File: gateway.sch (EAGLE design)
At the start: 25 parts, among them J1 RASPBERRYPI-40-PIN-GPIO_PTH_N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, Q1 BSS123

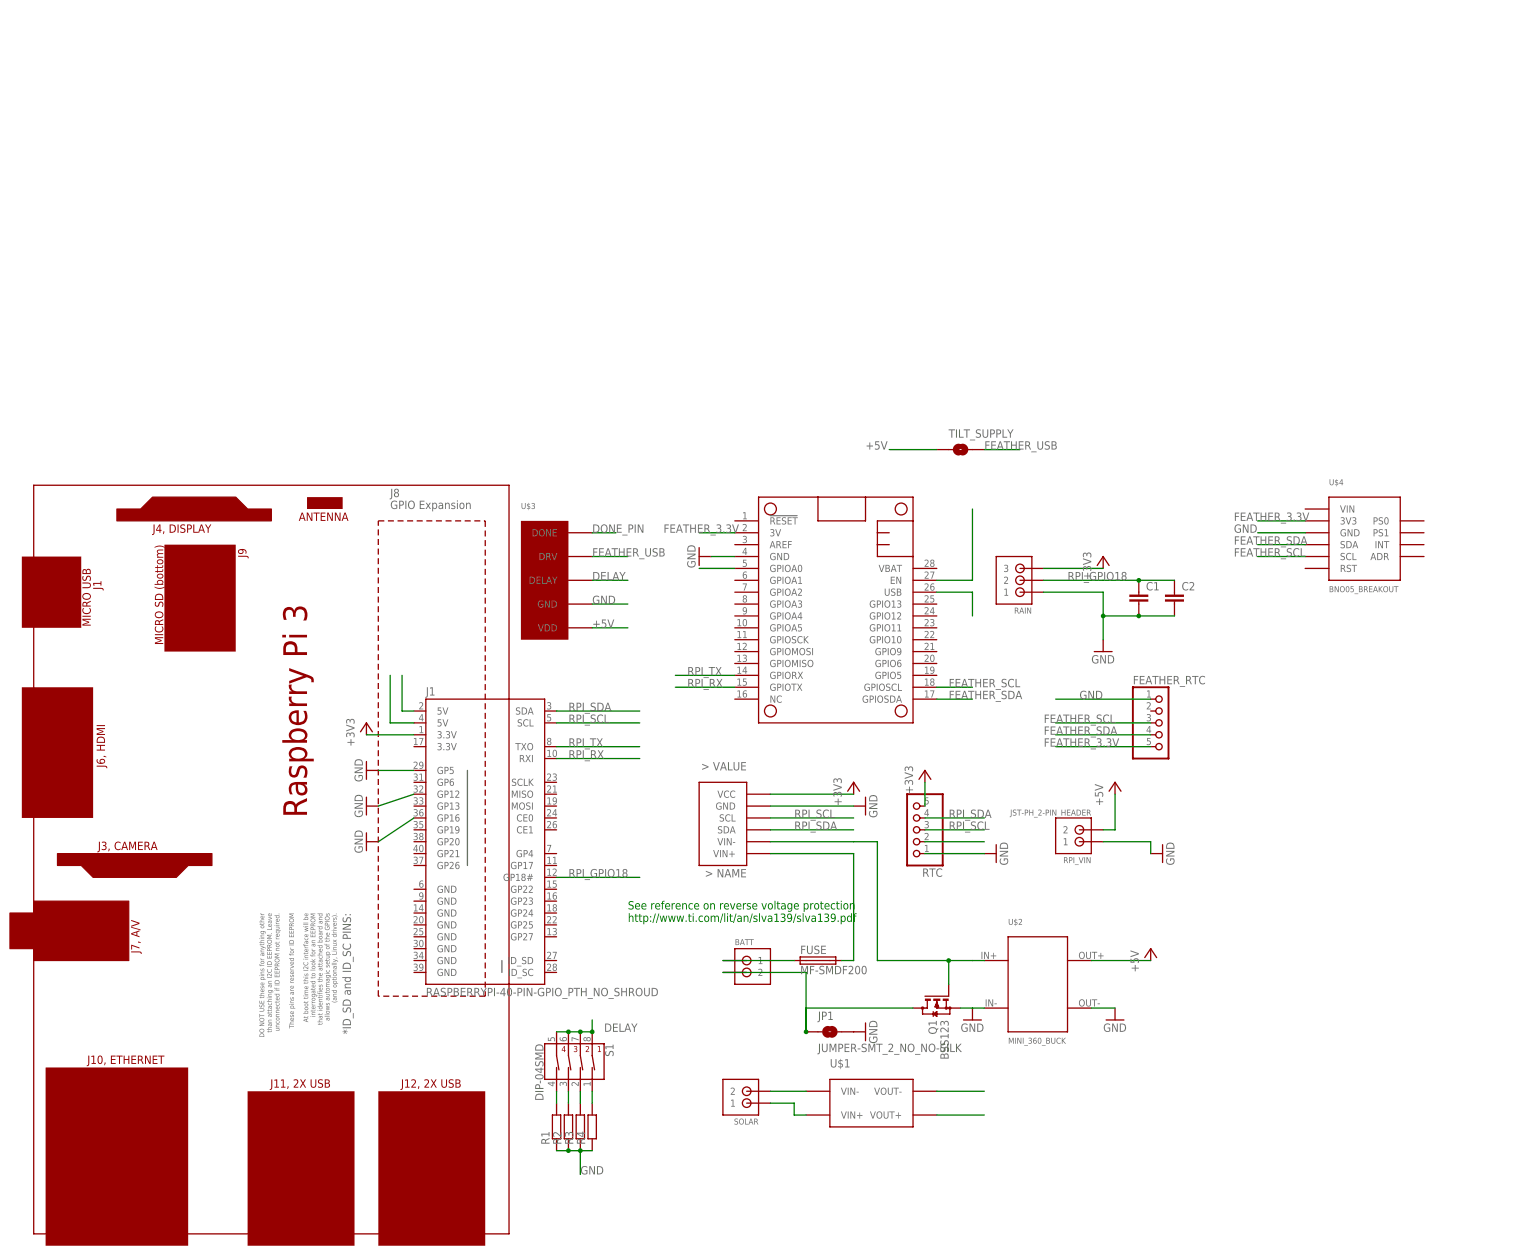
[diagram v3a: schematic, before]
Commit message: added pads to the microcontrollers ( feather and pi )
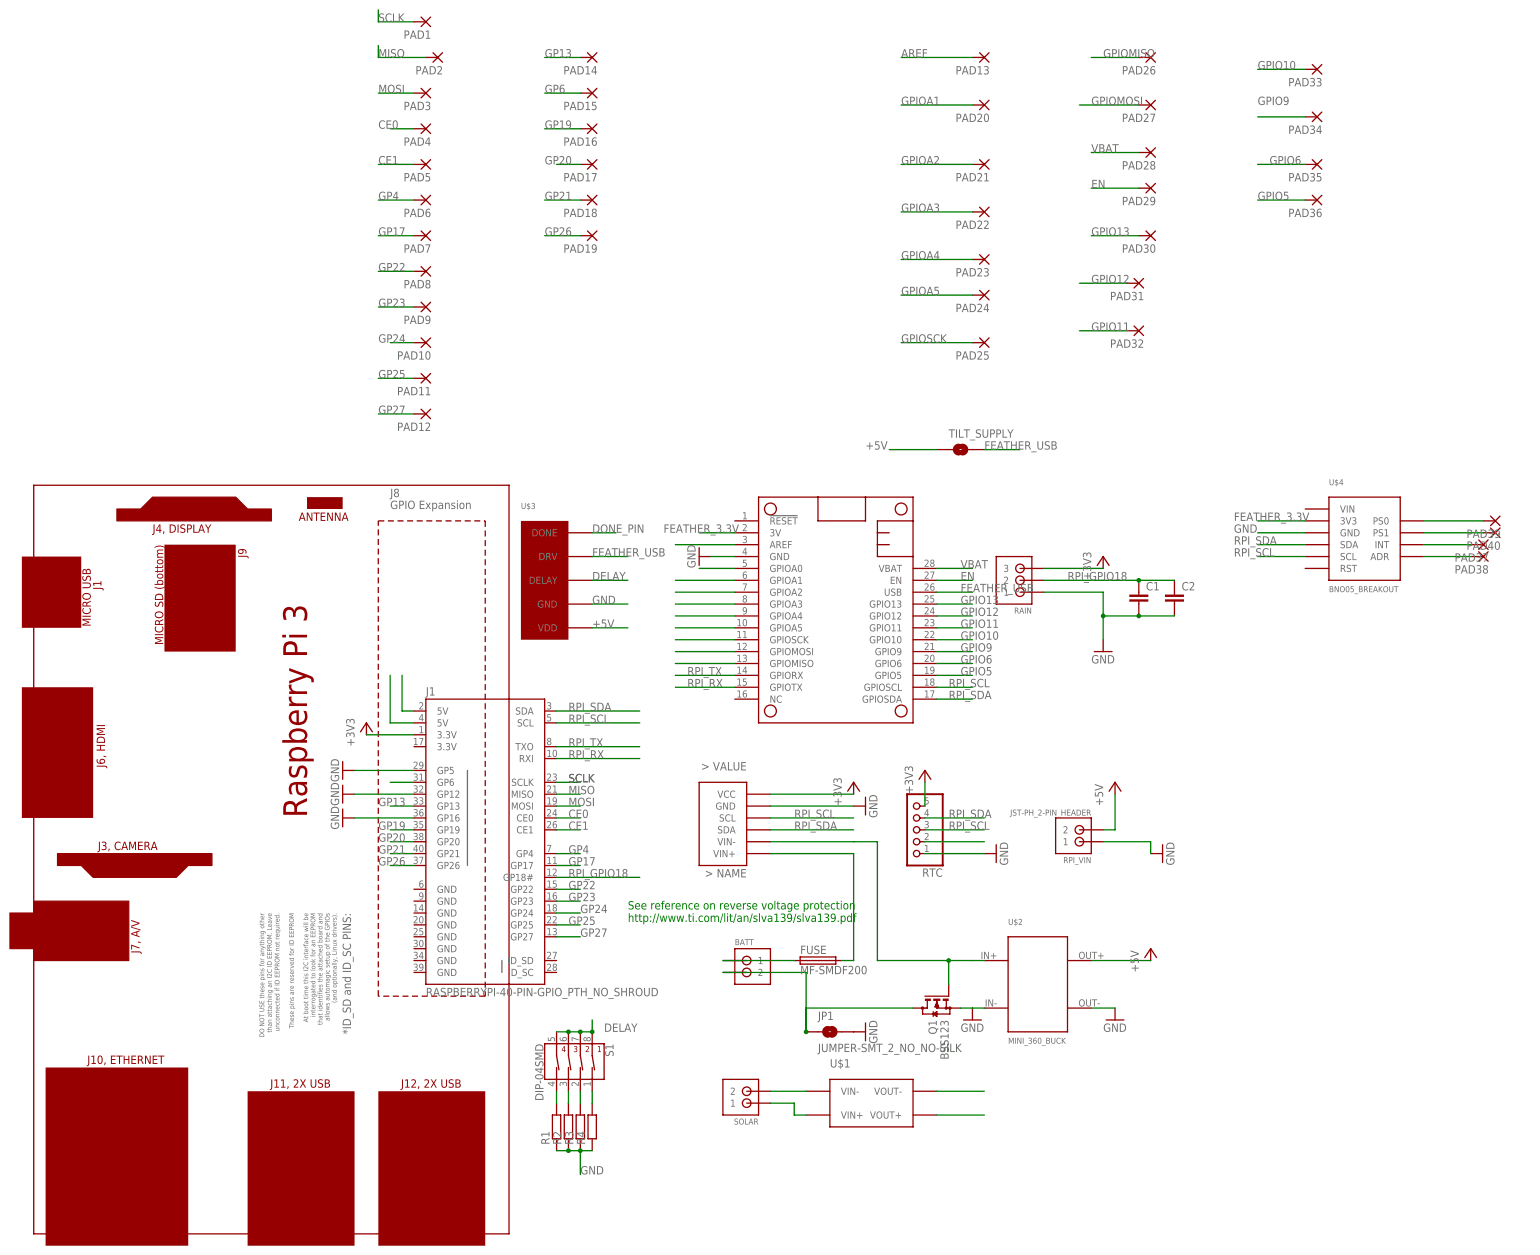
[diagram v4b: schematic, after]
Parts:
- removed FEATHER_RTC: (no value), pinhead:PINHD-1X5
- added PAD1, PAD10, PAD11, PAD12, PAD13, PAD14, PAD15, PAD16, PAD17, PAD18, PAD19, PAD2, PAD20, PAD21, PAD22, PAD23, PAD24, PAD25, PAD26, PAD27, PAD28, PAD29, PAD3, PAD30, PAD31, PAD32, PAD33, PAD34, PAD35, PAD36, PAD37, PAD38, PAD39, PAD4, PAD40, PAD5, PAD6, PAD7, PAD8, PAD9: WIREPADSMD1,27-254, wirepad:WIREPADSMD1,27-254
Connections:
- removed net FEATHER_SCL: FEATHER_RTC.3, MS1.GPIOSCL, U$4.SCL
- removed net FEATHER_SDA: FEATHER_RTC.4, MS1.GPIOSDA, U$4.SDA
- new net AREF: PAD13.P
- new net CE0: J1.CE0, PAD4.P
- new net CE1: J1.CE1, PAD5.P
- new net EN: MS1.EN, PAD29.P
- new net GP13: J1.GP13, PAD14.P
- new net GP17: J1.GP17, PAD7.P
- new net GP19: J1.GP19, PAD16.P
- new net GP20: J1.GP20, PAD17.P
- new net GP21: J1.GP21, PAD18.P
- new net GP22: J1.GP22, PAD8.P
- new net GP23: J1.GP23, PAD9.P
- new net GP24: J1.GP24, PAD10.P
- new net GP25: J1.GP25, PAD11.P
- new net GP26: J1.GP26, PAD19.P
- new net GP27: J1.GP27, PAD12.P
- new net GP4: J1.GP4, PAD6.P
- new net GP6: J1.GP6, PAD15.P
- new net GPIO10: MS1.GPIO10, PAD33.P
- new net GPIO11: MS1.GPIO11, PAD32.P
- new net GPIO12: MS1.GPIO12, PAD31.P
- new net GPIO13: MS1.GPIO13, PAD30.P
- new net GPIO5: MS1.GPIO5, PAD36.P
- new net GPIO6: MS1.GPIO6, PAD35.P
- new net GPIO9: MS1.GPIO9, PAD34.P
- new net GPIOA1: PAD20.P
- new net GPIOA2: MS1.GPIOA2, PAD21.P
- new net GPIOA3: MS1.GPIOA3, PAD22.P
- new net GPIOA4: MS1.GPIOA4, PAD23.P
- new net GPIOA5: MS1.GPIOA5, PAD24.P
- new net GPIOMISO: MS1.GPIOMISO, PAD26.P
- new net GPIOMOSI: MS1.GPIOMOSI, PAD27.P
- new net GPIOSCK: MS1.GPIOSCK, PAD25.P
- new net MISO: J1.MISO, PAD2.P
- new net MOSI: J1.MOSI, PAD3.P
- new net N$5: PAD38.P, U$4.ADR
- new net N$6: PAD39.P, U$4.PS0
- new net N$7: PAD40.P, U$4.PS1
- new net SCLK: J1.SCLK, PAD1.P
- new net VBAT: MS1.VBAT, PAD28.P
- net FEATHER_3.3V: no longer FEATHER_RTC.5
- net GND: no longer FEATHER_RTC.1
- net N$1: now also PAD37.P, U$4.INT; no longer MS1.EN
- net RPI_SCL: now also MS1.GPIOSCL, U$4.SCL
- net RPI_SDA: now also MS1.GPIOSDA, U$4.SDA

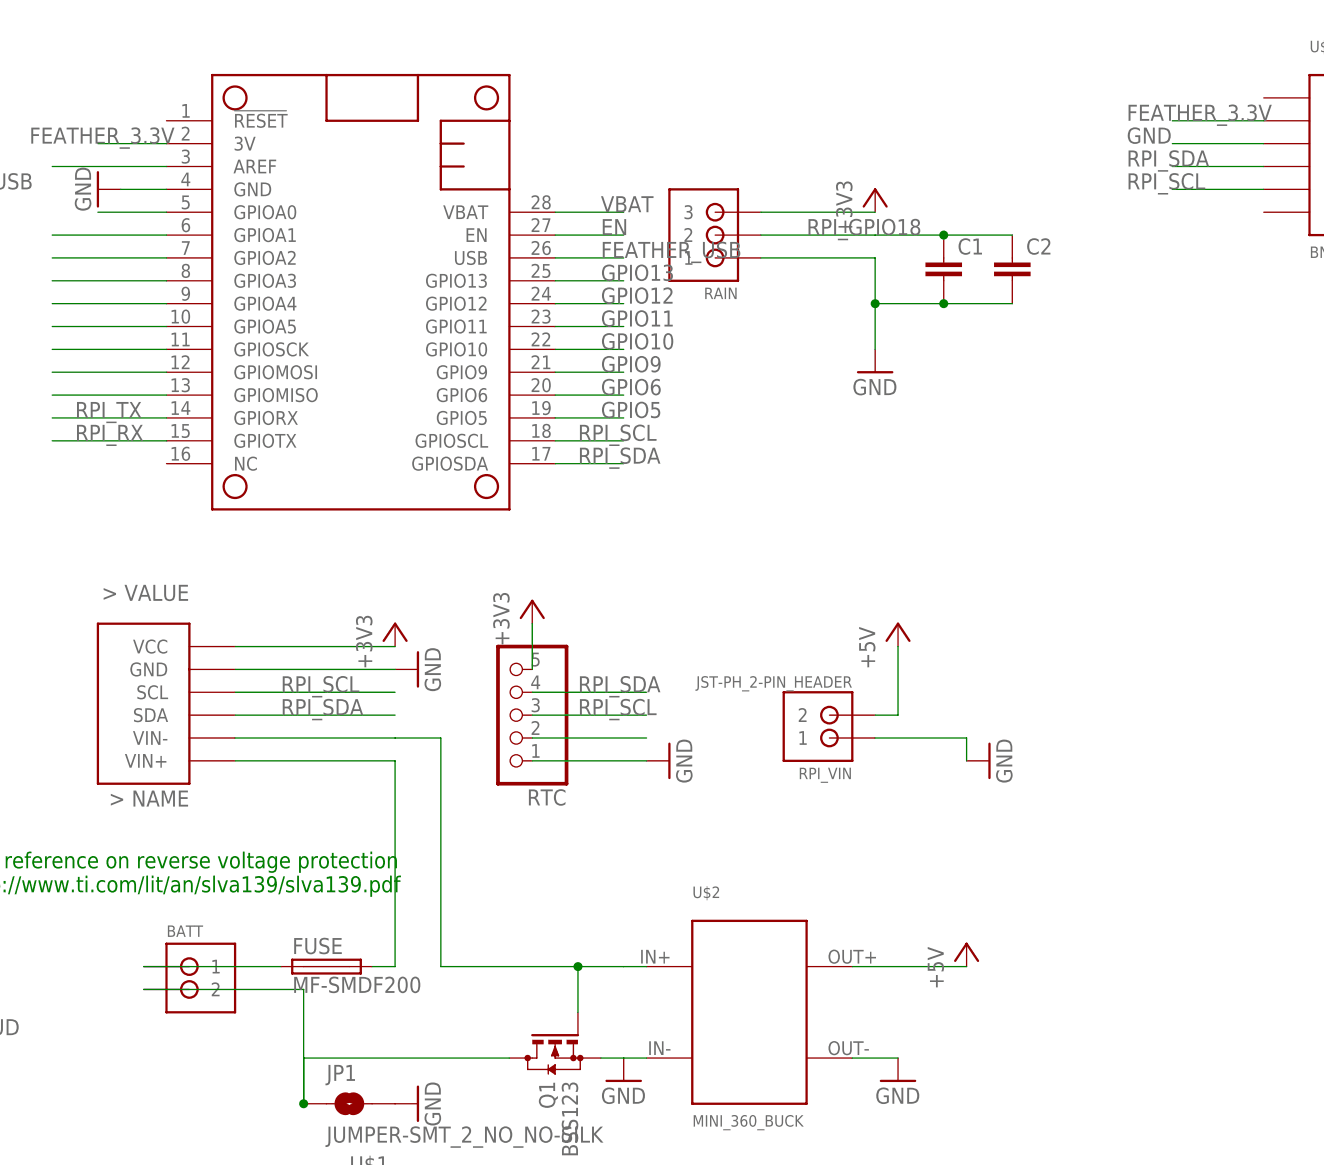
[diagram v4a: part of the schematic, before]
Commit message: added more fuse for more protection
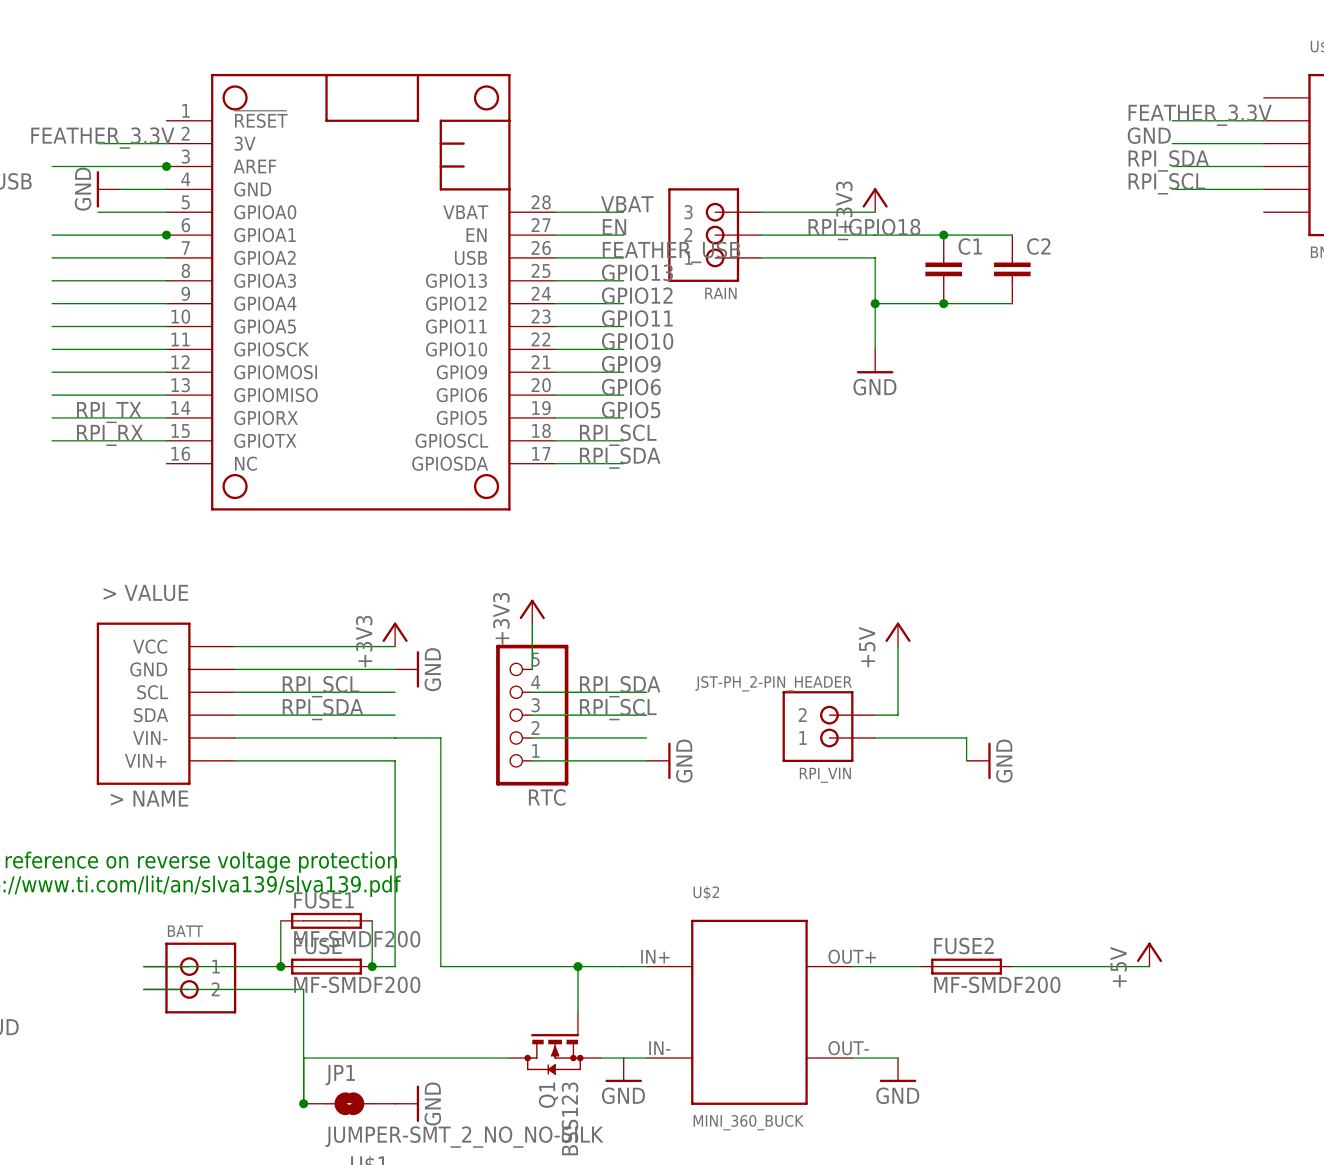
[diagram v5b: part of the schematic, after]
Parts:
- added FUSE1, FUSE2: MF-SMDF200, fuse:MF-SMDF200
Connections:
- new net N$8: FUSE2.1, U$2.VOUT+
- net +5V: now also FUSE2.2; no longer U$2.VOUT+
- net AREF: now also MS1.AREF
- net BATT+: now also FUSE1.1
- net GPIOA1: now also MS1.GPIOA1
- net INA_VIN+: now also FUSE1.2
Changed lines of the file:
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@@
 <part name="PAD39" library="wirepad" deviceset="WIREPAD" device="SMD1,27-254" value="WIREPADSMD1,27-254"/>
 <part name="PAD40" library="wirepad" deviceset="WIREPAD" device="SMD1,27-254" value="WIREPADSMD1,27-254"/>
+<part name="FUSE1" library="fuse" deviceset="MF-SMDF" device="" technology="200"/>
+<part name="FUSE2" library="fuse" deviceset="MF-SMDF" device="" technology="200"/>
 </parts>
 <sheets>
@@
 <instance part="P+1" gate="1" x="236.22" y="106.68"/>
 <instance part="GND9" gate="1" x="246.38" y="91.44" rot="R90"/>
-<instance part="P+2" gate="1" x="243.84" y="71.12"/>
+<instance part="P+2" gate="1" x="264.16" y="71.12"/>
 <instance part="JP1" gate="G$1" x="175.26" y="53.34"/>
 <instance part="GND10" gate="1" x="182.88" y="53.34" rot="R90"/>
@@
 <attribute name="NAME" x="318.643" y="158.1658" size="1.778" layer="95" rot="R180"/>
 </instance>
+<instance part="FUSE1" gate="A" x="172.72" y="73.66"/>
+<instance part="FUSE2" gate="A" x="243.84" y="68.58"/>
 </instances>
 <busses>
@@
 <pinref part="FUSE" gate="A" pin="1"/>
 <wire x1="152.4" y1="68.58" x2="167.64" y2="68.58" width="0.1524" layer="91"/>
+<pinref part="FUSE1" gate="A" pin="1"/>
+<wire x1="167.64" y1="73.66" x2="167.64" y2="68.58" width="0.1524" layer="91"/>
+<junction x="167.64" y="68.58"/>
 </segment>
 </net>
@@
 </segment>
 <segment>
-<wire x1="231.14" y1="68.58" x2="243.84" y2="68.58" width="0.1524" layer="91"/>
-<pinref part="P+2" gate="1" pin="+5V"/>
-<pinref part="U$2" gate="G$1" pin="VOUT+"/>
-</segment>
-<segment>
 <pinref part="U$3" gate="G$1" pin="VDD"/>
 <wire x1="124.46" y1="139.7" x2="132.08" y2="139.7" width="0.1524" layer="91"/>
@@
 <wire x1="198.12" y1="177.8" x2="187.96" y2="177.8" width="0.1524" layer="91"/>
 <label x="182.88" y="177.8" size="1.778" layer="95"/>
+</segment>
+<segment>
+<pinref part="FUSE2" gate="A" pin="2"/>
+<pinref part="P+2" gate="1" pin="+5V"/>
+<wire x1="248.92" y1="68.58" x2="264.16" y2="68.58" width="0.1524" layer="91"/>
 </segment>
 </net>
@@
 <wire x1="180.34" y1="68.58" x2="180.34" y2="91.44" width="0.1524" layer="91"/>
 <wire x1="180.34" y1="91.44" x2="162.56" y2="91.44" width="0.1524" layer="91"/>
+<pinref part="FUSE1" gate="A" pin="2"/>
+<wire x1="177.8" y1="73.66" x2="177.8" y2="68.58" width="0.1524" layer="91"/>
+<junction x="177.8" y="68.58"/>
 </segment>
 </net>
@@
 <segment>
 <wire x1="154.94" y1="149.86" x2="142.24" y2="149.86" width="0.1524" layer="91"/>
+<pinref part="MS1" gate="G$1" pin="GPIOA1"/>
+<junction x="154.94" y="149.86"/>
 </segment>
 <segment>
@@
 <segment>
 <wire x1="154.94" y1="157.48" x2="142.24" y2="157.48" width="0.1524" layer="91"/>
+<pinref part="MS1" gate="G$1" pin="AREF"/>
+<junction x="154.94" y="157.48"/>
 </segment>
 <segment>
@@
 </segment>
 </net>
+<net name="N$8" class="0">
+<segment>
+<pinref part="U$2" gate="G$1" pin="VOUT+"/>
+<pinref part="FUSE2" gate="A" pin="1"/>
+<wire x1="231.14" y1="68.58" x2="238.76" y2="68.58" width="0.1524" layer="91"/>
+</segment>
+</net>
